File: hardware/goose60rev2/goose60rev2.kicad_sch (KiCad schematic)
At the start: 14 parts, among them J1 USB_C_Receptacle_USB2.0_14P, J2 Conn_01x03_Pin, SW1 SW_Push, U1 RP2040, U3 W25Q128JVS, X1 12MHz

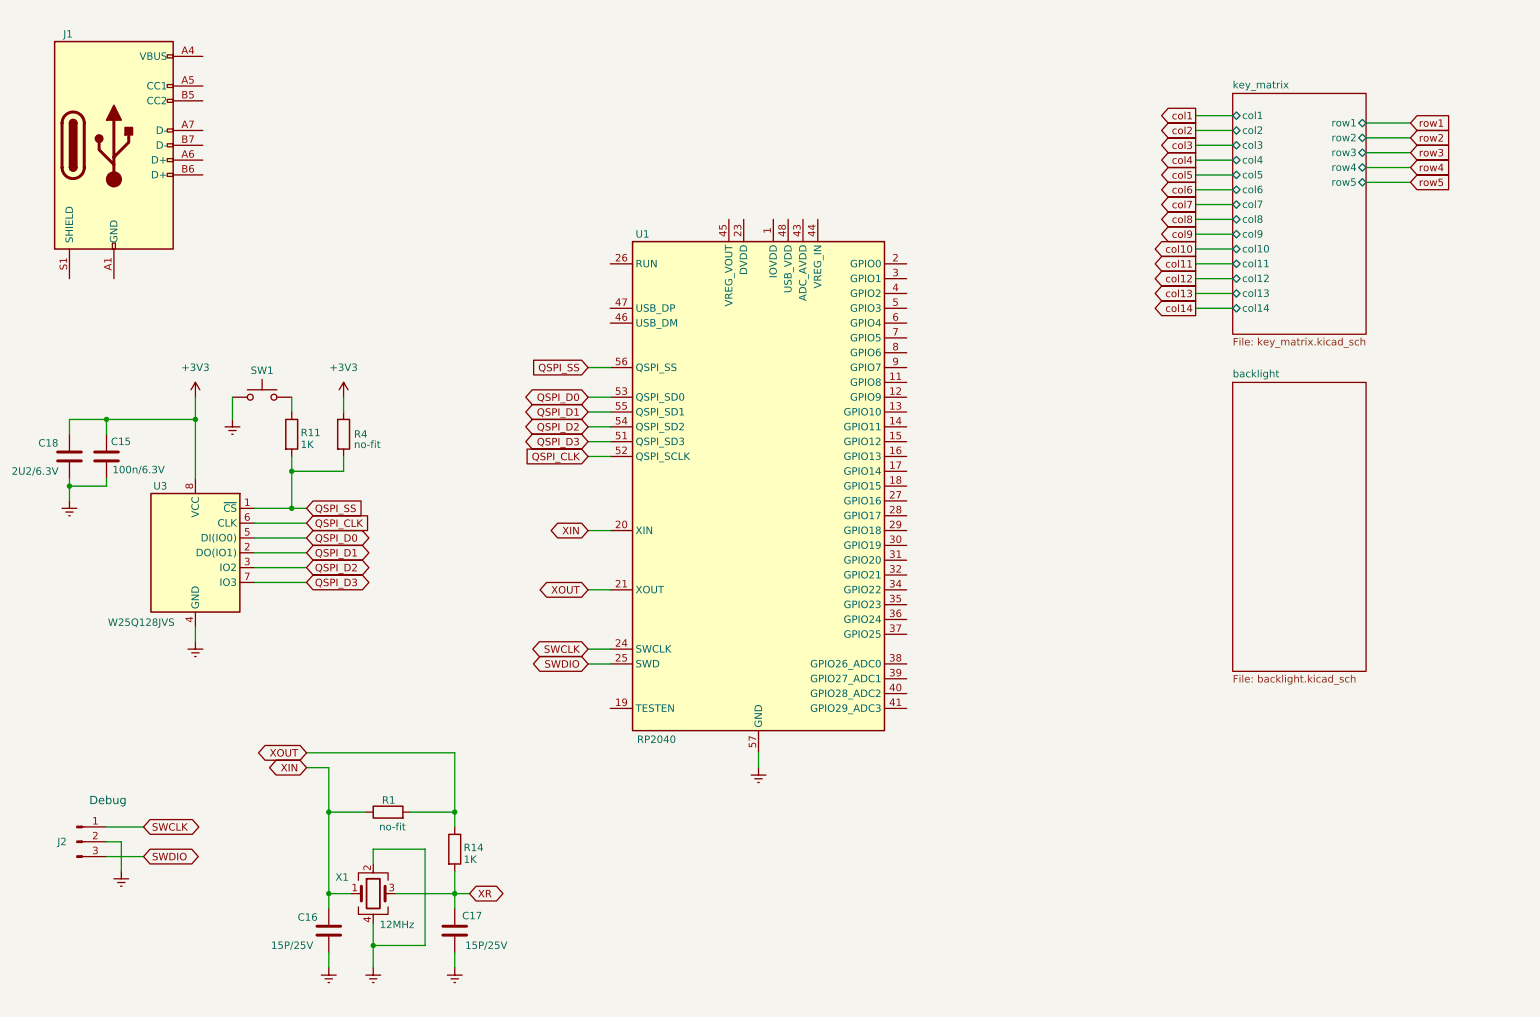
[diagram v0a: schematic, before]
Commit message: [WIP] modify sch design and add new connector
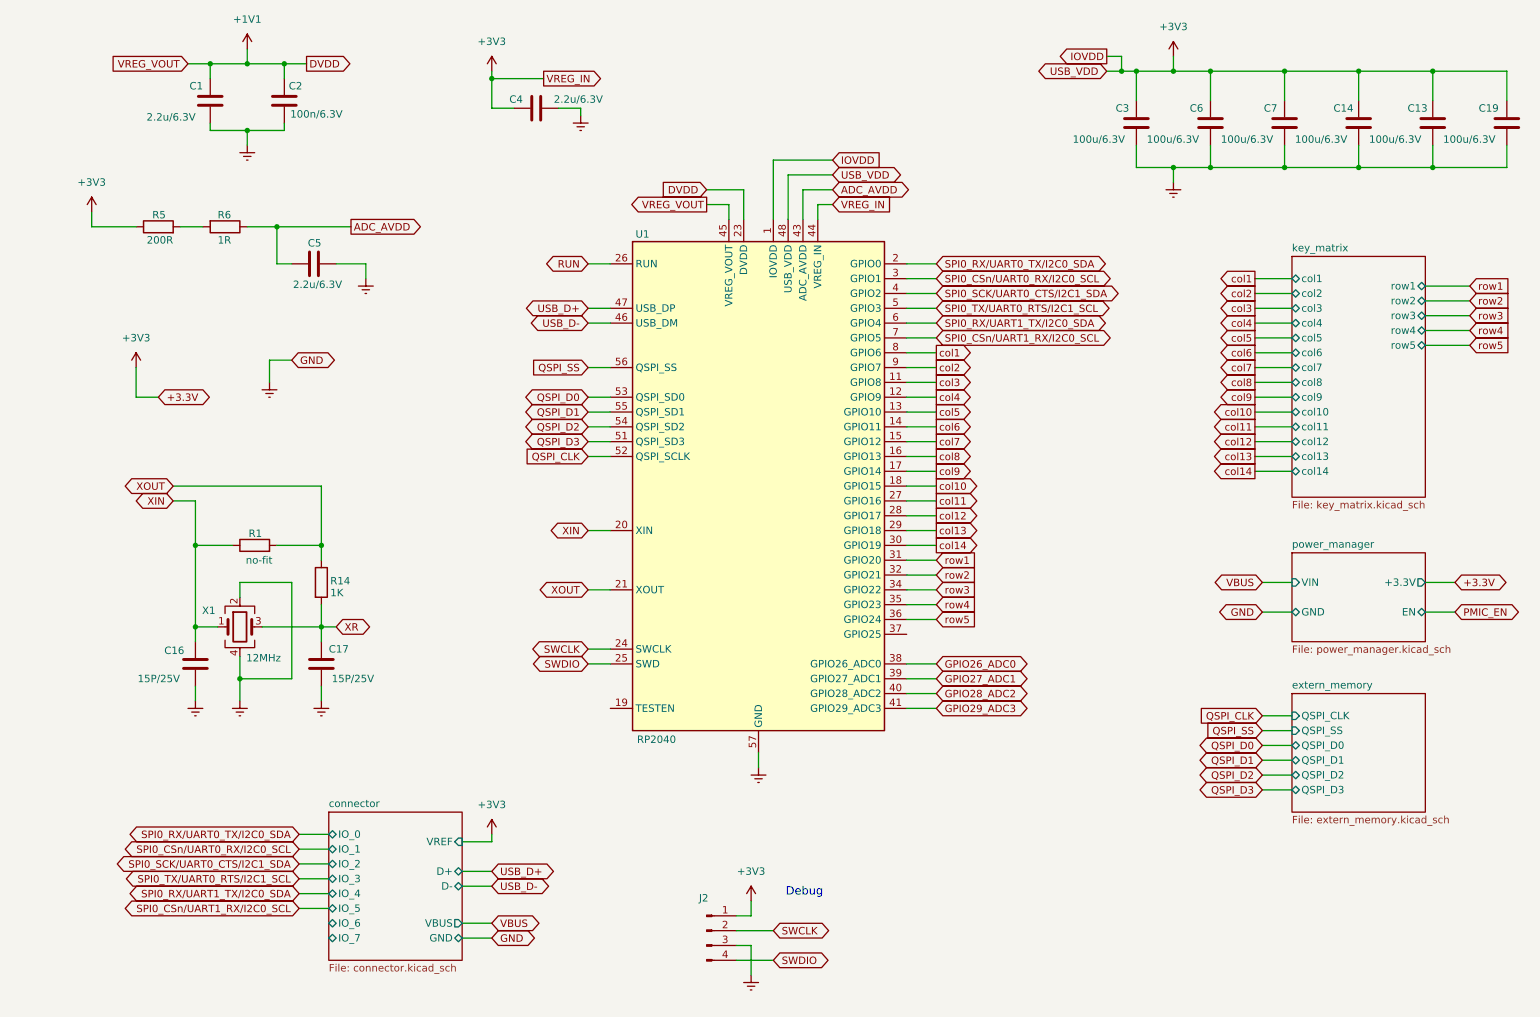
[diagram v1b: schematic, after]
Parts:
- removed C15: 100n/6.3V, Capacitor_SMD:C_0603_1608Metric_Pad1.08x0.95mm_HandSolder, symbol Device:C
- removed C18: 2U2/6.3V, Capacitor_SMD:C_0603_1608Metric_Pad1.08x0.95mm_HandSolder, symbol Device:C
- removed J1: USB_C_Receptacle_USB2.0_14P, symbol Connector:USB_C_Receptacle_USB2.0_14P
- removed J2: Conn_01x03_Pin, symbol Connector:Conn_01x03_Pin
- removed R11: 1K, symbol Device:R
- removed R4: no-fit, symbol Device:R
- removed SW1: SW_Push, symbol Switch:SW_Push
- removed U3: W25Q128JVS, Package_SO:SOIC-8_5.23x5.23mm_P1.27mm, symbol Memory_Flash:W25Q128JVS
- added C1, C4, C5: 2.2u/6.3V, Capacitor_SMD:C_0603_1608Metric_Pad1.08x0.95mm_HandSolder, symbol Device:C
- added C13, C14, C19, C3, C6, C7: 100u/6.3V, Capacitor_SMD:C_0603_1608Metric_Pad1.08x0.95mm_HandSolder, symbol Device:C
- added C2: 100n/6.3V, Capacitor_SMD:C_0603_1608Metric_Pad1.08x0.95mm_HandSolder, symbol Device:C
- added J2: Conn_01x04_Pin, symbol Connector:Conn_01x04_Pin
- added R5: 200R, symbol Device:R
- added R6: 1R, symbol Device:R
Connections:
- net GNDREF is gone; now on net GND: C16.2, C17.2, U1.57 (GND), X1.2, X1.4
- net +3V3: now also U1.1 (IOVDD), U1.10 (IOVDD), U1.22 (IOVDD), U1.33 (IOVDD), U1.42 (IOVDD), U1.44 (VREG_IN), U1.48 (USB_VDD), U1.49 (IOVDD), C13.1, C14.1, C19.1, C3.1, C4.1, C6.1, C7.1, J2.1 (Pin_1), R5.1
- net GND: now also C1.2, C13.2, C14.2, C19.2, C2.2, C3.2, C4.2, C5.2, C6.2, C7.2, J2.3 (Pin_3)
- net SWCLK: now also J2.2 (Pin_2)
- net SWDIO: now also J2.4 (Pin_4)
- net col1: now also U1.8 (GPIO6)
- net col10: now also U1.18 (GPIO15)
- net col11: now also U1.27 (GPIO16)
- net col12: now also U1.28 (GPIO17)
- net col13: now also U1.29 (GPIO18)
- net col14: now also U1.30 (GPIO19)
- net col2: now also U1.9 (GPIO7)
- net col3: now also U1.11 (GPIO8)
- net col4: now also U1.12 (GPIO9)
- net col5: now also U1.13 (GPIO10)
- net col6: now also U1.14 (GPIO11)
- net col7: now also U1.15 (GPIO12)
- net col8: now also U1.16 (GPIO13)
- net col9: now also U1.17 (GPIO14)
- net row1: now also U1.31 (GPIO20)
- net row2: now also U1.32 (GPIO21)
- net row3: now also U1.34 (GPIO22)
- net row4: now also U1.35 (GPIO23)
- net row5: now also U1.36 (GPIO24)
- net SPI0_RX/UART0_TX/I2C0_SDA: now reaches U1.2 (GPIO0)
- net +1V1: now reaches U1.23 (DVDD), U1.50 (DVDD)
- net +1V1: now also U1.45 (VREG_VOUT), C1.1, C2.1
- net RUN: now reaches U1.26 (RUN)
- net SPI0_CSn/UART0_RX/I2C0_SCL: now reaches U1.3 (GPIO1)
- net GPIO26_ADC0: now reaches U1.38 (GPIO26_ADC0)
- net GPIO27_ADC1: now reaches U1.39 (GPIO27_ADC1)
- net SPI0_SCK/UART0_CTS/I2C1_SDA: now reaches U1.4 (GPIO2)
- net GPIO28_ADC2: now reaches U1.40 (GPIO28_ADC2)
- net GPIO29_ADC3: now reaches U1.41 (GPIO29_ADC3)
- net ADC_AVDD: now reaches U1.43 (ADC_AVDD)
- net ADC_AVDD: now also C5.1, R6.1
- net USB_D-: now reaches U1.46 (USB_DM)
- net USB_D+: now reaches U1.47 (USB_DP)
- net SPI0_TX/UART0_RTS/I2C1_SCL: now reaches U1.5 (GPIO3)
- net SPI0_RX/UART1_TX/I2C0_SDA: now reaches U1.6 (GPIO4)
- net SPI0_CSn/UART1_RX/I2C0_SCL: now reaches U1.7 (GPIO5)
- new net: R5.2, R6.2
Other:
- removed sheet backlight
- added sheet connector (connector.kicad_sch)
- added sheet extern_memory (extern_memory.kicad_sch)
- added sheet power_manager (power_manager.kicad_sch)
- moved on the sheet: C16, C17, R1, R14, X1

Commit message: update sch design
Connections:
- net GPIO28_ADC2 is gone; now on net VIN_ADC: U1.40 (GPIO28_ADC2)
- net RUN is gone; now on net +3V3: U1.26 (RUN)
- net GND: now also U1.19 (TESTEN)
- net SUBPWR_EN: now reaches U1.37 (GPIO25)
- net GPIO27_ADC1 renamed VIN_ADC
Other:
- sheet connector ports: added ADC0, ADC1; removed none
- sheet power_manager ports: added VIN_ADC; removed none

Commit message: update conn packages
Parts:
- J2: footprint (none) -> Connector_PinHeader_2.54mm:PinHeader_1x04_P2.54mm_Vertical
- R1, R14, R5, R6: footprint (none) -> Resistor_SMD:R_0603_1608Metric
- X1: footprint (none) -> Crystal:Crystal_SMD_TXC_7M-4Pin_3.2x2.5mm
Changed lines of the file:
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@@
 			)
 		)
-		(property "Footprint" ""
+		(property "Footprint" "Crystal:Crystal_SMD_TXC_7M-4Pin_3.2x2.5mm"
 			(at 53.34 121.92 0)
 			(effects
@@
 			)
 		)
-		(property "Footprint" ""
+		(property "Footprint" "Resistor_SMD:R_0603_1608Metric"
 			(at 55.88 109.728 90)
 			(effects
@@
 			)
 		)
-		(property "Footprint" ""
+		(property "Footprint" "Resistor_SMD:R_0603_1608Metric"
 			(at 65.532 114.3 90)
 			(effects
@@
 			)
 		)
-		(property "Footprint" ""
+		(property "Footprint" "Resistor_SMD:R_0603_1608Metric"
 			(at 39.37 55.118 90)
 			(effects
@@
 			)
 		)
-		(property "Footprint" ""
+		(property "Footprint" "Resistor_SMD:R_0603_1608Metric"
 			(at 50.8 51.562 90)
 			(effects
@@
 			)
 		)
-		(property "Footprint" ""
+		(property "Footprint" "Connector_PinHeader_2.54mm:PinHeader_1x04_P2.54mm_Vertical"
 			(at 133.35 173.99 0)
 			(effects
